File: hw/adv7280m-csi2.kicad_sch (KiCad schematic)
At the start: 72 parts, among them J1 RPi_CSI_15pin, J2 CVBS_RCA, J4 5V_IN, J5 CVBS_IN_HDR, J6 MON1_HDR, J7 MON2_HDR, J8 CVBS_BUF_HDR, U1 ADV7280WBCPZ-M, U2 AP2112K-1.8, U3 AP2112K-1.8, U5 THS7314DR, Y1 28.63636MHz

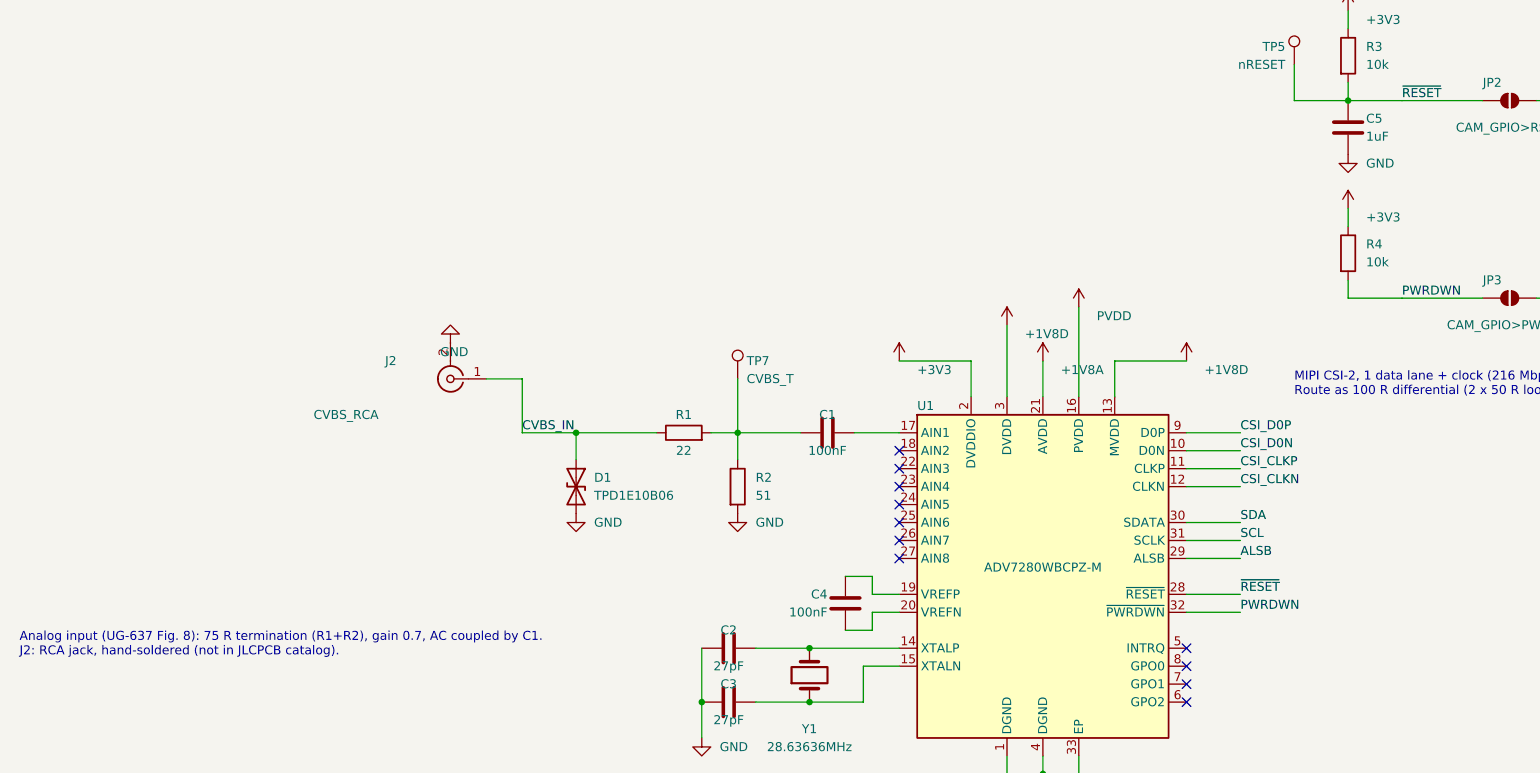
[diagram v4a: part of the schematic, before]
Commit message: Stage 5b: buffer section placement (42x55 board, breakaway slot with two tabs), RESET C5 4.7 uF, render script
- gen_pcb.py: outline with 2 mm slot and 2.5 mm tabs, placement of THS7314 section, silkscreen, rev B
- route_pcb.py: zones cover the whole outline
- C5 1 uF -> 4.7 uF (tau 47 ms, RESET low >= 13 ms); UG-637 figure reference fixed
- tools/render.sh regenerates docs/render-*.png and layer images
- assumptions A5-5 decided, A5-9 added; docs updated

Co-Authored-By: Claude Fable 5.1 <noreply@anthropic.com>
Claude-Session: https://claude.ai/code/session_017Xy941kmWX9XJsHmZMcZcK
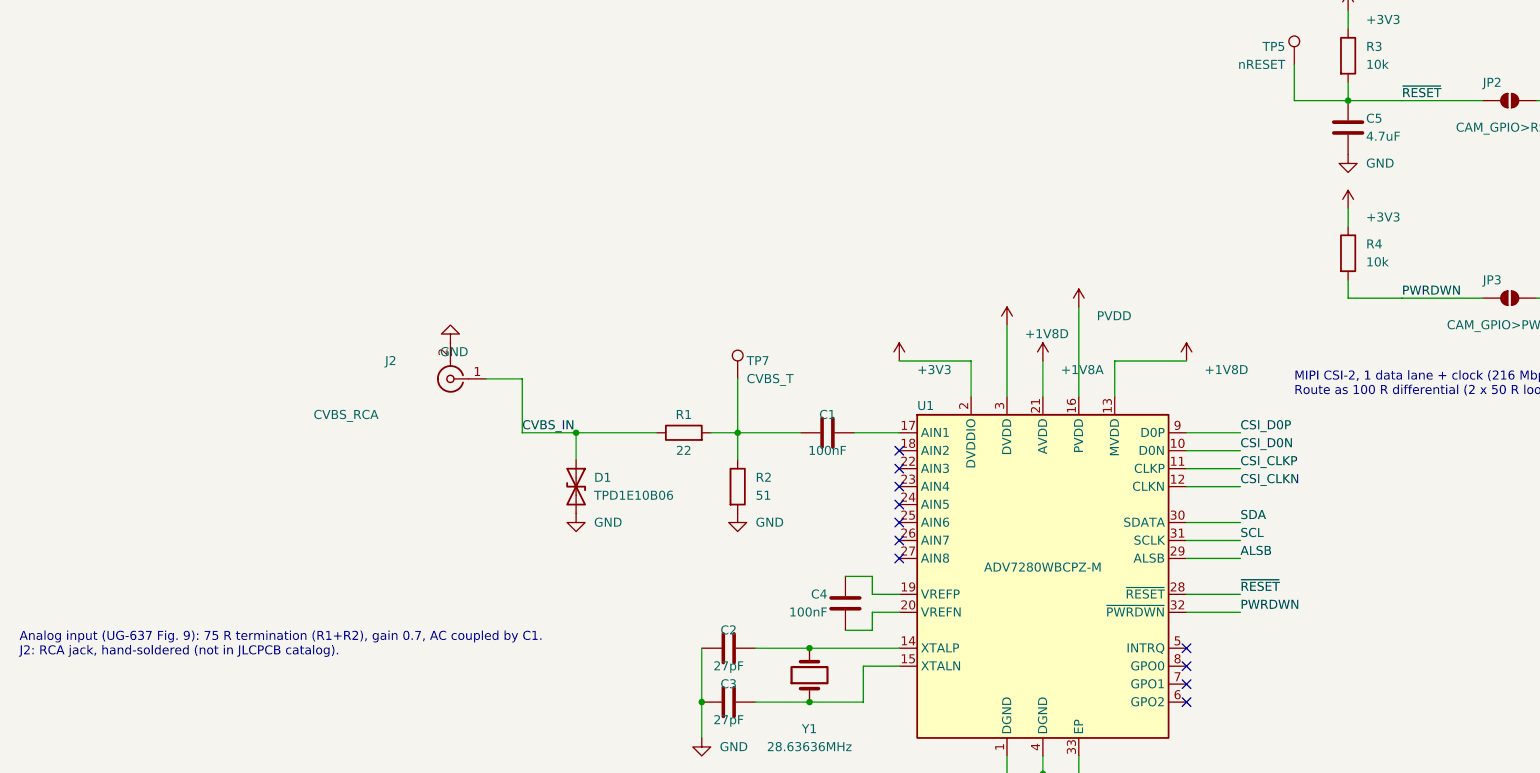
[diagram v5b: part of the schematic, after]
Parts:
- C5: value 1uF -> 4.7uF; LCSC C15849 -> C19666
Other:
- note added: "Analog input (UG-637 Fig. 9): 75 R termination (R1+R2), gain 0.7, AC coupled by C1. J2: RCA jack, hand-soldered (not in JLCPCB catalog)."
- note removed: "Analog input (UG-637 Fig. 8): 75 R termination (R1+R2), gain 0.7, AC coupled by C1. J2: RCA jack, hand-soldered (not in JLCPCB catalog)."
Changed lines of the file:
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@@
 		)
 	)
-	(text "Analog input (UG-637 Fig. 8): 75 R termination (R1+R2), gain 0.7, AC coupled by C1.\nJ2: RCA jack, hand-soldered (not in JLCPCB catalog)."
+	(text "Analog input (UG-637 Fig. 9): 75 R termination (R1+R2), gain 0.7, AC coupled by C1.\nJ2: RCA jack, hand-soldered (not in JLCPCB catalog)."
 		(exclude_from_sim no)
 		(at 55.88 140.97 0)
@@
 			)
 		)
-		(property "Description" "Series termination (24 R in UG-637 Fig. 8; 22 R = nearest JLCPCB Basic)"
+		(property "Description" "Series termination (24 R in UG-637 Fig. 9; 22 R = nearest JLCPCB Basic)"
 			(at 149.86 109.22 0)
 			(effects
@@
 			)
 		)
-		(property "Value" "1uF"
+		(property "Value" "4.7uF"
 			(at 246.38 67.31 0)
 			(effects
@@
 			)
 		)
-		(property "Description" "RESET RC, tau = 10 ms (>5 ms min)"
+		(property "Description" "RESET RC, tau = 47 ms: low (<0.8 V) for 13 ms after 3V3 (>5 ms min), high (>2 V) at 44 ms"
 			(at 243.84 66.04 0)
 			(effects
@@
 			)
 		)
-		(property "LCSC" "C15849"
+		(property "LCSC" "C19666"
 			(at 243.84 66.04 0)
 			(effects

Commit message: Rev C (SPRUT-2 case): one board, JST connectors, final routing, fab outputs
Board and parts
- One solid 42x55 mm board (no breakaway section); JST-PH video in/out (J5 in,
  J6 TV, J7 GX16) and JST-XH 5 V (J4) on the edges; buffer CH1 hard-wired to the
  decoder input (RCA J2, J8, JP4, D1 removed).
- U1 ADV7280BCPZ-M (C662255) assembled by JLCPCB; LDO input caps C29/C30 1 uF.
- KiCad 10 on Windows: generator paths, field transfer for KiCad 10 DRC,
  portable fab.sh, .gitattributes keeps *.sh LF.

Routing (docs/routing-rules.md, audit items 1-18)
- MIPI CSI-2 as loosely coupled pairs 0.30/0.45 mm (101 R diff, 29 R common
  mode); both lines of each pair get 2 vias, GND return vias at every layer
  change, lengths matched (P = N, 0.2 mm between pairs).
- In2 GND everywhere with compact power zones; every B.Cu signal (MIPI hops,
  I2C, CAM_GPIO) runs over one plane; CAM_GPIO clears the H1 mounting hole.
- Video 75 R: 0.13 mm with a 0.4 mm pour gap (hw/adv7280m-csi2.kicad_dru).
- Crystal turned 90 deg right under pins 14/15 (XTALN 2.8 mm), load caps at
  its pads, nothing under it; 10 nF next to every supply pin, plane after the
  100 nF; PVDD feed on B.Cu around the crystal.
- U1 exposed pad: own footprint with 4 paste windows (60 %) and 5 vias
  0.45/0.2 mm in the paste-free cross.
- ERC 0, check_nets OK, DRC (all severities, schematic parity) 0/0/0.

Docs and outputs
- Gerber/drill, JLCPCB BOM/CPL, schematic PDF/PNG, renders, layer images,
  STEP/DXF regenerated; assumptions A6-1..A6-16; docs/bring-up.md (first
  power-up to ustreamer); tools/zsolve.py impedance solver.

Co-Authored-By: Claude Opus 5.5 <noreply@anthropic.com>
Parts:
- removed D1: TPD1E10B06, adv-parts:TI_X1SON-2_DPY0002A_1.0x0.6mm, symbol Device:D_TVS
- removed J2: CVBS_RCA, adv-parts:RCA_Multicomp_PSG01546_Horizontal, symbol Connector:Conn_Coaxial
- removed J8: CVBS_BUF_HDR, Connector_PinHeader_2.54mm:PinHeader_1x02_P2.54mm_Vertical, symbol Connector_Generic:Conn_01x02
- removed JP4: BUF>ADV, Jumper:SolderJumper-2_P1.3mm_Bridged_RoundedPad1.0x1.5mm, symbol Jumper:SolderJumper_2_Bridged
- added C29, C30: 1uF, Capacitor_SMD:C_0402_1005Metric, symbol Device:C
- J4: footprint TerminalBlock_Phoenix:TerminalBlock_Phoenix_MKDS-1,5-2-5.08_1x02_P5.08mm_Horizontal -> Connector_JST:JST_XH_S2B-XH-A_1x02_P2.50mm_Horizontal; symbol Connector:Screw_Terminal_01x02 -> Connector_Generic:Conn_01x02; LCSC C474881 -> C157931; MPN KF301-5.0-2P -> S2B-XH-A(LF)(SN)
- J5: value CVBS_IN_HDR -> CVBS_IN; footprint Connector_PinHeader_2.54mm:PinHeader_1x02_P2.54mm_Vertical -> Connector_JST:JST_PH_S2B-PH-K_1x02_P2.00mm_Horizontal; LCSC C492401 -> C173752; MPN PZ254V-11-02P -> S2B-PH-K-S(LF)(SN)
- J6: value MON1_HDR -> TV; footprint Connector_PinHeader_2.54mm:PinHeader_1x02_P2.54mm_Vertical -> Connector_JST:JST_PH_S2B-PH-K_1x02_P2.00mm_Horizontal; LCSC C492401 -> C173752; MPN PZ254V-11-02P -> S2B-PH-K-S(LF)(SN)
- J7: value MON2_HDR -> GX16; footprint Connector_PinHeader_2.54mm:PinHeader_1x02_P2.54mm_Vertical -> Connector_JST:JST_PH_S2B-PH-K_1x02_P2.00mm_Horizontal; LCSC C492401 -> C173752; MPN PZ254V-11-02P -> S2B-PH-K-S(LF)(SN)
- U1: value ADV7280WBCPZ-M -> ADV7280BCPZ-M; footprint Package_DFN_QFN:QFN-32-1EP_5x5mm_P0.5mm_EP3.6x3.6mm -> adv-parts:QFN-32-1EP_5x5mm_P0.5mm_EP3.6x3.6mm_Paste4; Assemble no -> (none); LCSC C662261 -> C662255; MPN ADV7280WBCPZ-M -> ADV7280BCPZ-M
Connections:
- net CVBS_BUF is gone; now on net CVBS_IN: R9.2
- net +3V3: now also C29.1, C30.1
- net GND: now also C29.2, C30.2
- net MON1 renamed TV_OUT
- net MON2 renamed GX16_OUT
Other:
- note added: "5 V from the case DC-DC 5 V module via J4 (JST-XH); the Pi 4 is powered from the same module. The decoder itself runs from the Pi 3.3 V (J1 pin 15). Panel BNC -> coax -> J5 -> buffer: CH1 -> decoder, CH2 -> J6 TV (AV in), CH3 -> J7 GX16 monitor."
- note added: "Analog input (UG-637 Fig. 9): 75 R termination (R1+R2), gain 0.7, AC coupled by C1. CVBS_IN is driven by THS7314 CH1 through R9 (75 R); ESD protection is at the board input (D3)."
- note added: "Input (SLOS513A Fig. 33/34): R8 75 R termination, D3 ESD, C23-C25 100 nF series -> sync-tip clamp (DC restore) mode, one cap per input (each input has its own clamp). Outputs: gain 6 dB (x2), series 75 R into 75 R load -> unity overall. CH1 -> decoder (R1+R2 = 73 R load), CH2/CH3 -> J6 TV / J7 GX16. Bandwidth 8.5 MHz (5th-order LPF)."
- note added: "MIPI CSI-2, 1 data lane + clock (216 Mbps interlaced / 432 Mbps I2P). Route as 100 R differential (2 x 50 R loosely coupled per UG-637), GND plane under; P/N crossover: both lines 2 vias + GND return vias."
- note added: "THS7314 BUFFER STAGE (rev C: one board for the SPRUT-2 case)"
- note removed: "5 V from the external DC-DC module via J4 (screw terminal); the Pi 4 is powered from the same 5 V by its own cable. Only two copper links cross the tabs: CVBS_IN and GND. Snap off -> J8 -> cable -> J2 (RCA) on the decoder board."
- note removed: "Analog input (UG-637 Fig. 9): 75 R termination (R1+R2), gain 0.7, AC coupled by C1. J2: RCA jack, hand-soldered (not in JLCPCB catalog)."
- note removed: "CVBS_IN: copper track across the breakaway tab to the decoder input node (J2 / D1 / R1). Cut JP4 to feed J2 directly while the boards are joined; when snapped off use J8."
- note removed: "Input (SLOS513A Fig. 33/34): R8 75 R termination, D3 ESD, C23-C25 100 nF series -> sync-tip clamp (DC restore) mode, one cap per input (each input has its own clamp). Outputs: gain 6 dB (x2), series 75 R into 75 R load -> unity overall. CH1 -> decoder (JP4 bridged), CH2/CH3 -> monitors J6/J7. Bandwidth 8.5 MHz (5th-order LPF)."
- note removed: "MIPI CSI-2, 1 data lane + clock (216 Mbps interlaced / 432 Mbps I2P). Route as 100 R differential (2 x 50 R loosely coupled per UG-637), no vias, GND plane under."
- note removed: "THS7314 BUFFER STAGE - separable section (breakaway tabs, see PCB)"
- title: CVBS to MIPI CSI-2 video decoder (ADV7280-M) for Raspberry Pi 4 -> CVBS to MIPI CSI-2 decoder ADV7280-M, Pi 4, SPRUT-2

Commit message: Rev C: breakaway buffer section, solder pads instead of JST, СПРУТ-М label
- Buffer section snaps off again: 2 mm slot at y 32..34 with two tabs
  (x 7.0..9.5 GND only, x 31.15..33.65 GND + CVBS_IN). While joined the video
  runs over the tab; when split, a coax is soldered between J8 "TO ADV"
  (buffer) and J2 "CVBS" (decoder). D1 TPD1E10B06 ESD back at the decoder input.
- No connectors on the board: J4 (5 V), J5 (CVBS in), J6 TV, J7 GX16, J2, J8
  are plated solder holes (PinHeader_1x02, 1.0 mm), not assembled, no 3D model;
  pin 1 kept in place, routing unchanged. JST parts removed from the BOM.
- Mounting holes: decoder H1 (8.0; 3.2) / H2 (39.5; 27.5), buffer
  H3 (3.2; 51.8) / H4 (39.5; 37.0) - each section diagonal.
- Silkscreen: product name "СПРУТ-М".
- ERC 0, check_nets OK, DRC (all severities, schematic parity) 0/0/0; MIPI
  lengths, In2 planes under B.Cu and 75 R video unchanged.
- Fab outputs, STEP/DXF, renders, schematic PNG, README, enclosure dims,
  bring-up guide (split + soldering steps), assumptions A6-17, A6-18.

Co-Authored-By: Claude Opus 5.5 <noreply@anthropic.com>
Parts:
- added D1: TPD1E10B06, adv-parts:TI_X1SON-2_DPY0002A_1.0x0.6mm, symbol Device:D_TVS
- added J2: CVBS_PADS, Connector_PinHeader_2.54mm:PinHeader_1x02_P2.54mm_Vertical, symbol Connector_Generic:Conn_01x02
- added J8: TO_ADV_PADS, Connector_PinHeader_2.54mm:PinHeader_1x02_P2.54mm_Vertical, symbol Connector_Generic:Conn_01x02
- J4: footprint Connector_JST:JST_XH_S2B-XH-A_1x02_P2.50mm_Horizontal -> Connector_PinHeader_2.54mm:PinHeader_1x02_P2.54mm_Vertical; LCSC C157931 -> (none); MPN S2B-XH-A(LF)(SN) -> (none)
- J5, J6, J7: footprint Connector_JST:JST_PH_S2B-PH-K_1x02_P2.00mm_Horizontal -> Connector_PinHeader_2.54mm:PinHeader_1x02_P2.54mm_Vertical; LCSC C173752 -> (none); MPN S2B-PH-K-S(LF)(SN) -> (none)
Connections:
- net CVBS_IN: now also D1.1 (A1), J2.1 (Pin_1), J8.1 (Pin_1)
- net GND: now also D1.2 (A2), J2.2 (Pin_2), J8.2 (Pin_2)
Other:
- note added: "5 V from the case DC-DC 5 V module via J4 (solder pads); the Pi 4 is powered from the same module. The decoder itself runs from the Pi 3.3 V (J1 pin 15). Panel BNC -> coax -> J5 -> buffer: CH1 -> decoder, CH2 -> J6 TV (AV in), CH3 -> J7 GX16 monitor."
- note added: "Analog input (UG-637 Fig. 9): 75 R termination (R1+R2), gain 0.7, AC coupled by C1. CVBS_IN is driven by THS7314 CH1 through R9 (75 R) across the breakaway tab; when split: J8 -> coax -> J2, D1 = ESD at J2."
- note added: "THS7314 BUFFER STAGE (rev C: breakaway section, SPRUT-2 case)"
- note removed: "5 V from the case DC-DC 5 V module via J4 (JST-XH); the Pi 4 is powered from the same module. The decoder itself runs from the Pi 3.3 V (J1 pin 15). Panel BNC -> coax -> J5 -> buffer: CH1 -> decoder, CH2 -> J6 TV (AV in), CH3 -> J7 GX16 monitor."
- note removed: "Analog input (UG-637 Fig. 9): 75 R termination (R1+R2), gain 0.7, AC coupled by C1. CVBS_IN is driven by THS7314 CH1 through R9 (75 R); ESD protection is at the board input (D3)."
- note removed: "THS7314 BUFFER STAGE (rev C: one board for the SPRUT-2 case)"
